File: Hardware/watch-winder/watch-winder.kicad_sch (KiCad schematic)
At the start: 28 parts, among them J1 SWD, J2 UART, J3 MOT, SW1 SW_Push, U1 STM32F030K6Tx, U2 M24C02-FMN, U3 ULN2003, Y1 8M

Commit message: add sync ios
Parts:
- added J4: SYNC0, Connector_PinHeader_2.54mm:PinHeader_1x03_P2.54mm_Vertical, symbol Connector:Conn_01x03_Pin
- added J5: SYNC1, Connector_PinHeader_2.54mm:PinHeader_1x03_P2.54mm_Vertical, symbol Connector:Conn_01x03_Pin
- added R10, R11: 220R, Resistor_SMD:R_0805_2012Metric_Pad1.20x1.40mm_HandSolder, symbol Device:R
- added R12, R13: 2k2, Resistor_SMD:R_0805_2012Metric_Pad1.20x1.40mm_HandSolder, symbol Device:R
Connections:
- net +3V3: now also R12.2, R13.2
- net +5V: now also J4.1 (Pin_1), J5.1 (Pin_1)
- net GND: now also J4.3 (Pin_3), J5.3 (Pin_3)
- net SYNC0: now reaches U1.18 (PA8)
- net SYNC0: now also R10.1, R12.1
- net SYNC1: now reaches U1.21 (PA11)
- net SYNC1: now also R11.1, R13.1
- new net: J4.2 (Pin_2), R10.2
- new net: J5.2 (Pin_2), R11.2

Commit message: add button/led connectors
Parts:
- added J6: BUTTON0, Connector_PinHeader_2.54mm:PinHeader_1x03_P2.54mm_Vertical, symbol Connector:Conn_01x03_Pin
- added J7: BUTTON1, Connector_PinHeader_2.54mm:PinHeader_1x03_P2.54mm_Vertical, symbol Connector:Conn_01x03_Pin
- added J8: LED2, Connector_PinSocket_2.54mm:PinSocket_1x02_P2.54mm_Vertical, symbol Connector:Conn_01x02_Pin
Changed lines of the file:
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@@
+	)
+	(symbol
+		(lib_id "Connector:Conn_01x02_Pin")
+		(at 196.85 127 0)
+		(mirror y)
+		(unit 1)
+		(exclude_from_sim no)
+		(in_bom yes)
+		(on_board yes)
+		(dnp no)
+		(fields_autoplaced yes)
+		(property "Reference" "J8"
+			(at 198.12 126.9999 0)
+			(effects
+				(font
+					(size 1.27 1.27)
+				)
+				(justify right)
+			)
+		)
+		(property "Value" "LED2"
+			(at 198.12 129.5399 0)
+			(effects
+				(font
+					(size 1.27 1.27)
+				)
+				(justify right)
+			)
+		)
+		(property "Footprint" "Connector_PinSocket_2.54mm:PinSocket_1x02_P2.54mm_Vertical"
+			(at 196.85 127 0)
+			(effects
+				(font
+					(size 1.27 1.27)
+				)
+				(hide yes)
+			)
+		)
+		(property "Datasheet" "~"
+			(at 196.85 127 0)
+			(effects
+				(font
+					(size 1.27 1.27)
+				)
+				(hide yes)
+			)
+		)
+		(property "Description" "Generic connector, single row, 01x02, script generated"
+			(at 196.85 127 0)
+			(effects
+				(font
+					(size 1.27 1.27)
+				)
+				(hide yes)
+			)
+		)
+		(pin "2"
+		)
+		(pin "1"
+		)
+		(instances
+			(project "watch-winder"
+				(path "/e4615983-86dc-4379-93ce-772c86486517"
+					(reference "J8")
+					(unit 1)
+				)
+			)
+		)
 	)
 	(symbol
@@
 	)
 	(symbol
+		(lib_id "Connector:Conn_01x03_Pin")
+		(at 196.85 110.49 0)
+		(mirror y)
+		(unit 1)
+		(exclude_from_sim no)
+		(in_bom yes)
+		(on_board yes)
+		(dnp no)
+		(fields_autoplaced yes)
+		(property "Reference" "J6"
+			(at 198.12 109.2199 0)
+			(effects
+				(font
+					(size 1.27 1.27)
+				)
+				(justify right)
+			)
+		)
+		(property "Value" "BUTTON0"
+			(at 198.12 111.7599 0)
+			(effects
+				(font
+					(size 1.27 1.27)
+				)
+				(justify right)
+			)
+		)
+		(property "Footprint" "Connector_PinHeader_2.54mm:PinHeader_1x03_P2.54mm_Vertical"
+			(at 196.85 110.49 0)
+			(effects
+				(font
+					(size 1.27 1.27)
+				)
+				(hide yes)
+			)
+		)
+		(property "Datasheet" "~"
+			(at 196.85 110.49 0)
+			(effects
+				(font
+					(size 1.27 1.27)
+				)
+				(hide yes)
+			)
+		)
+		(property "Description" "Generic connector, single row, 01x03, script generated"
+			(at 196.85 110.49 0)
+			(effects
+				(font
+					(size 1.27 1.27)
+				)
+				(hide yes)
+			)
+		)
+		(pin "1"
+		)
+		(pin "2"
+		)
+		(pin "3"
+		)
+		(instances
+			(project ""
+				(path "/e4615983-86dc-4379-93ce-772c86486517"
+					(reference "J6")
+					(unit 1)
+				)
+			)
+		)
+	)
+	(symbol
 		(lib_id "power:GND")
 		(at 124.46 125.73 0)
@@
 					(unit 1)
 				)
+			)
+		)
+	)
+	(symbol
+		(lib_id "Connector:Conn_01x03_Pin")
+		(at 196.85 119.38 0)
+		(mirror y)
+		(unit 1)
+		(exclude_from_sim no)
+		(in_bom yes)
+		(on_board yes)
+		(dnp no)
+		(fields_autoplaced yes)
+		(property "Reference" "J7"
+			(at 198.12 118.1099 0)
+			(effects
+				(font
+					(size 1.27 1.27)
+				)
+				(justify right)
+			)
+		)
+		(property "Value" "BUTTON1"
+			(at 198.12 120.6499 0)
+			(effects
+				(font
+					(size 1.27 1.27)
+				)
+				(justify right)
+			)
+		)
+		(property "Footprint" "Connector_PinHeader_2.54mm:PinHeader_1x03_P2.54mm_Vertical"
+			(at 196.85 119.38 0)
+			(effects
+				(font
+					(size 1.27 1.27)
+				)
+				(hide yes)
+			)
+		)
+		(property "Datasheet" "~"
+			(at 196.85 119.38 0)
+			(effects
+				(font
+					(size 1.27 1.27)
+				)
+				(hide yes)
+			)
+		)
+		(property "Description" "Generic connector, single row, 01x03, script generated"
+			(at 196.85 119.38 0)
+			(effects
+				(font
+					(size 1.27 1.27)
+				)
+				(hide yes)
+			)
+		)
+		(pin "1"
+		)
+		(pin "2"
+		)
+		(pin "3"
+		)
+		(instances
+			(project "watch-winder"
+				(path "/e4615983-86dc-4379-93ce-772c86486517"
+					(reference "J7")
+					(unit 1)
+				)

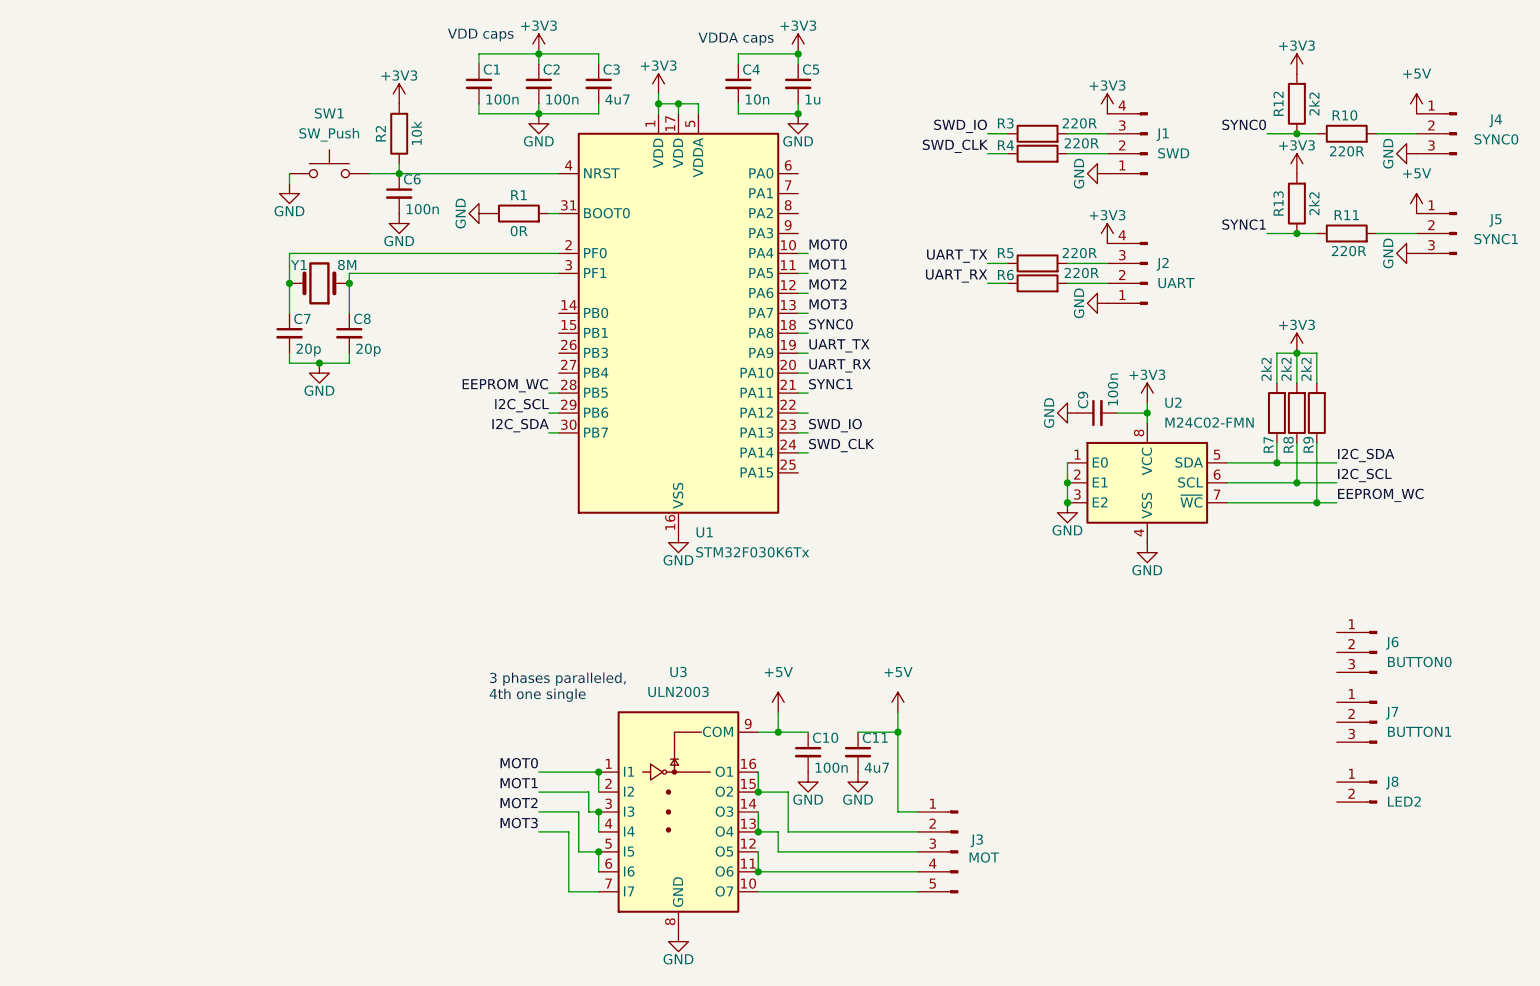
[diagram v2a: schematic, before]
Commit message: add leds and buttons
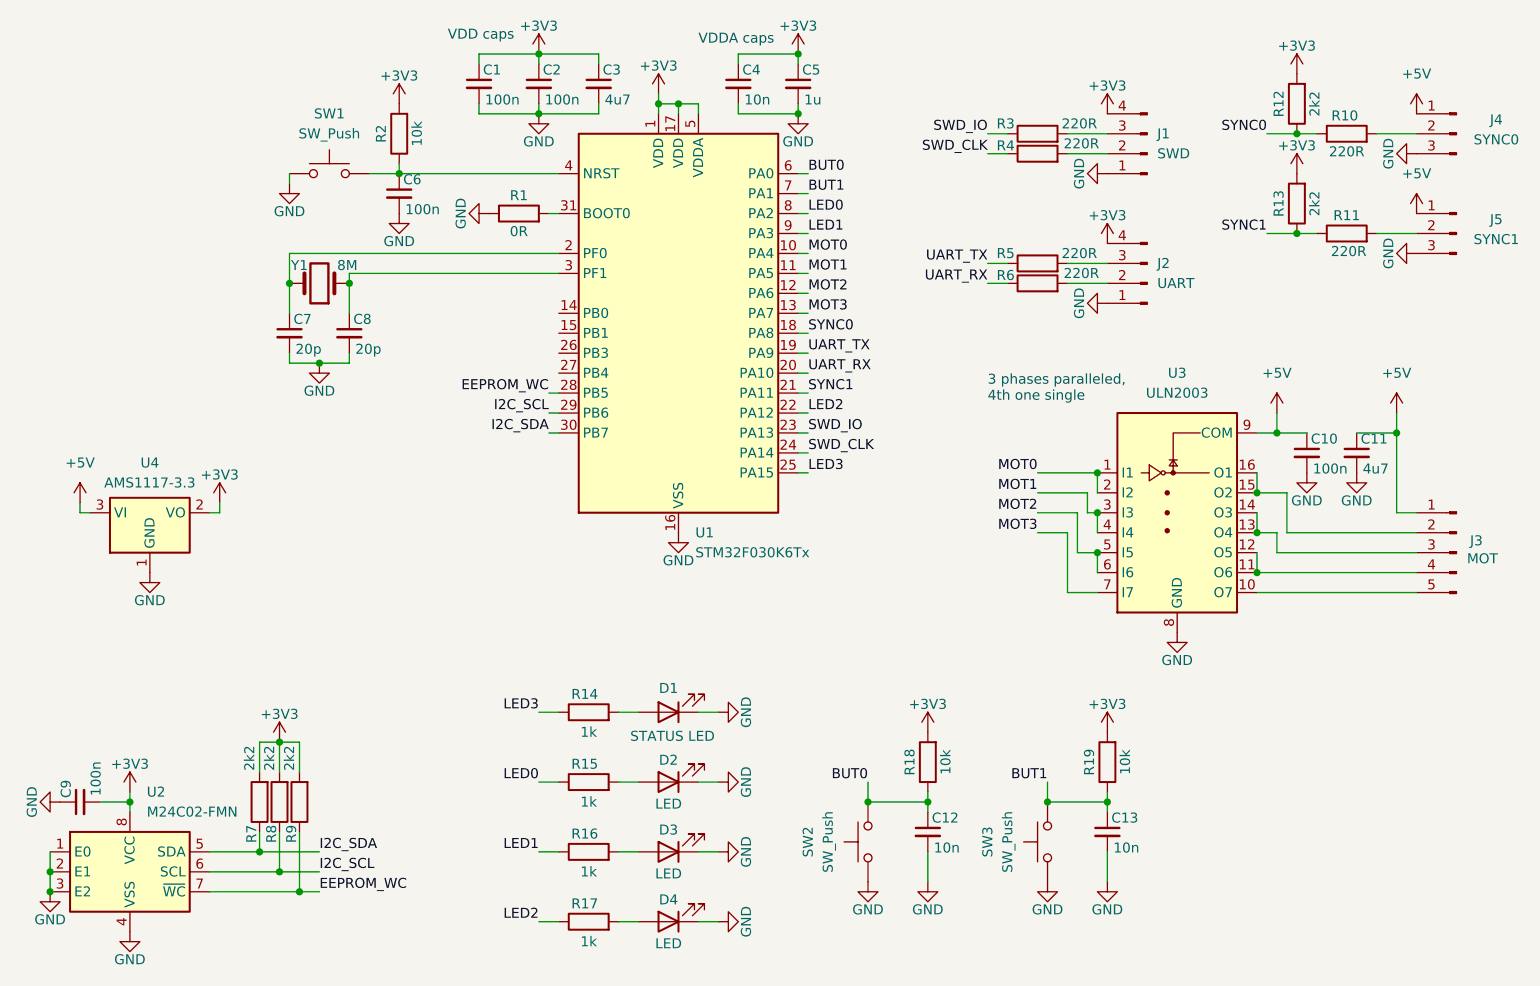
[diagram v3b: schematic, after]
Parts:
- removed J6: BUTTON0, Connector_PinHeader_2.54mm:PinHeader_1x03_P2.54mm_Vertical, symbol Connector:Conn_01x03_Pin
- removed J7: BUTTON1, Connector_PinHeader_2.54mm:PinHeader_1x03_P2.54mm_Vertical, symbol Connector:Conn_01x03_Pin
- removed J8: LED2, Connector_PinSocket_2.54mm:PinSocket_1x02_P2.54mm_Vertical, symbol Connector:Conn_01x02_Pin
- added C12, C13: 10n, Capacitor_SMD:C_0805_2012Metric_Pad1.18x1.45mm_HandSolder, symbol Device:C_Small
- added D1: STATUS LED, LED_SMD:LED_0805_2012Metric_Pad1.15x1.40mm_HandSolder, symbol Device:LED
- added D2, D3, D4: LED, LED_THT:LED_D5.0mm, symbol Device:LED
- added R14, R15, R16, R17: 1k, Resistor_SMD:R_0805_2012Metric_Pad1.20x1.40mm_HandSolder, symbol Device:R
- added R18, R19: 10k, Resistor_SMD:R_0805_2012Metric_Pad1.20x1.40mm_HandSolder, symbol Device:R
- added SW2, SW3: SW_Push, Button_Switch_THT:SW_PUSH_6mm, symbol Switch:SW_Push
- added U4: AMS1117-3.3, Package_TO_SOT_SMD:SOT-223-3_TabPin2, symbol Regulator_Linear:AMS1117-3.3
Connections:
- net +3V3: now also R18.2, R19.2, U4.2 (VO)
- net +5V: now also U4.3 (VI)
- net GND: now also C12.2, C13.2, D1.1 (K), D2.1 (K), D3.1 (K), D4.1 (K), SW2.1, SW3.1, U4.1 (GND)
- net LED2: now reaches U1.22 (PA12)
- net LED2: now also R17.1
- net LED3: now reaches U1.25 (PA15)
- net LED3: now also R14.1
- net BUT0: now reaches U1.6 (PA0)
- net BUT0: now also C12.1, R18.1, SW2.2
- net BUT1: now reaches U1.7 (PA1)
- net BUT1: now also C13.1, R19.1, SW3.2
- net LED0: now reaches U1.8 (PA2)
- net LED0: now also R15.1
- net LED1: now reaches U1.9 (PA3)
- net LED1: now also R16.1
- new net: D2.2 (A), R15.2
- new net: D4.2 (A), R17.2
- new net: D3.2 (A), R16.2
- new net: D1.2 (A), R14.2
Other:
- moved on the sheet: C10, C11, C9, J3, R7, R8, R9, U2, U3

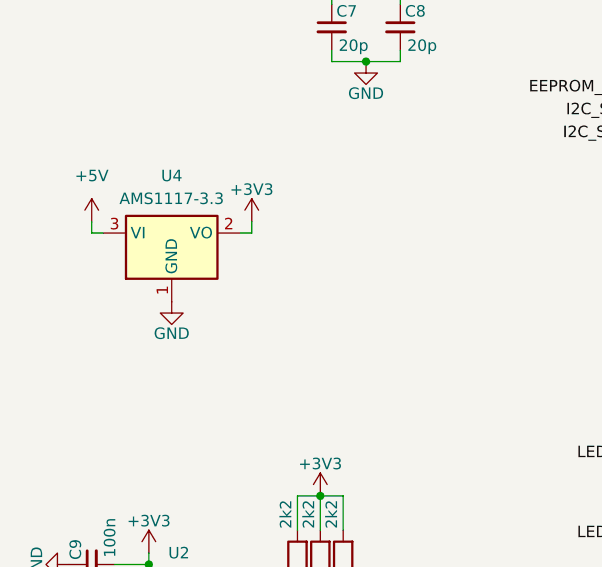
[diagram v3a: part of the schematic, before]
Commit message: add power section
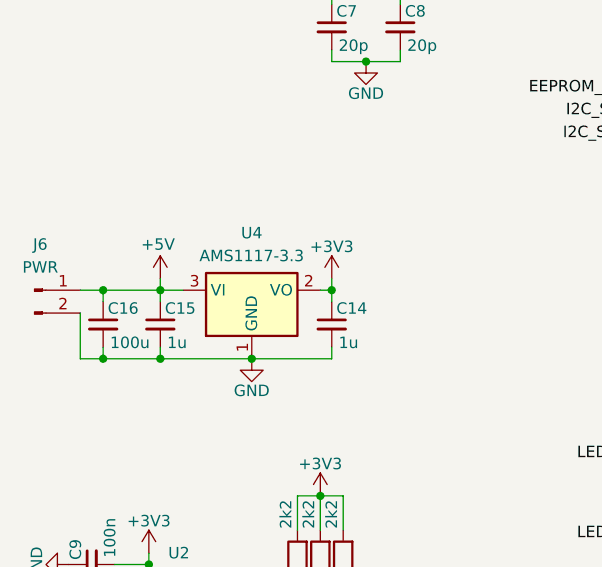
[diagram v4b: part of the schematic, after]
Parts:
- added C14, C15: 1u, Capacitor_SMD:C_0805_2012Metric_Pad1.18x1.45mm_HandSolder, symbol Device:C_Small
- added C16: 100u, Capacitor_THT:C_Radial_D5.0mm_H5.0mm_P2.00mm, symbol Device:C_Small
- added J6: PWR, Connector_PinHeader_2.54mm:PinHeader_1x02_P2.54mm_Horizontal, symbol Connector:Conn_01x02_Pin
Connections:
- net +3V3: now also C14.1
- net +5V: now also C15.1, C16.1, J6.1 (Pin_1)
- net GND: now also C14.2, C15.2, C16.2, J6.2 (Pin_2)
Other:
- moved on the sheet: U4
